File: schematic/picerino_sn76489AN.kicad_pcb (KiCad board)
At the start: 2 copper layers, 83.8 x 53.5 mm, 23 parts, among them CON1 PICERINO-EDGE, J1 Conn_01x02, J2 Conn_01x02, J3 Conn_01x02, U1 sn76489an, U2 74LS00, U3 LM386, Y1 3.579545Mhz

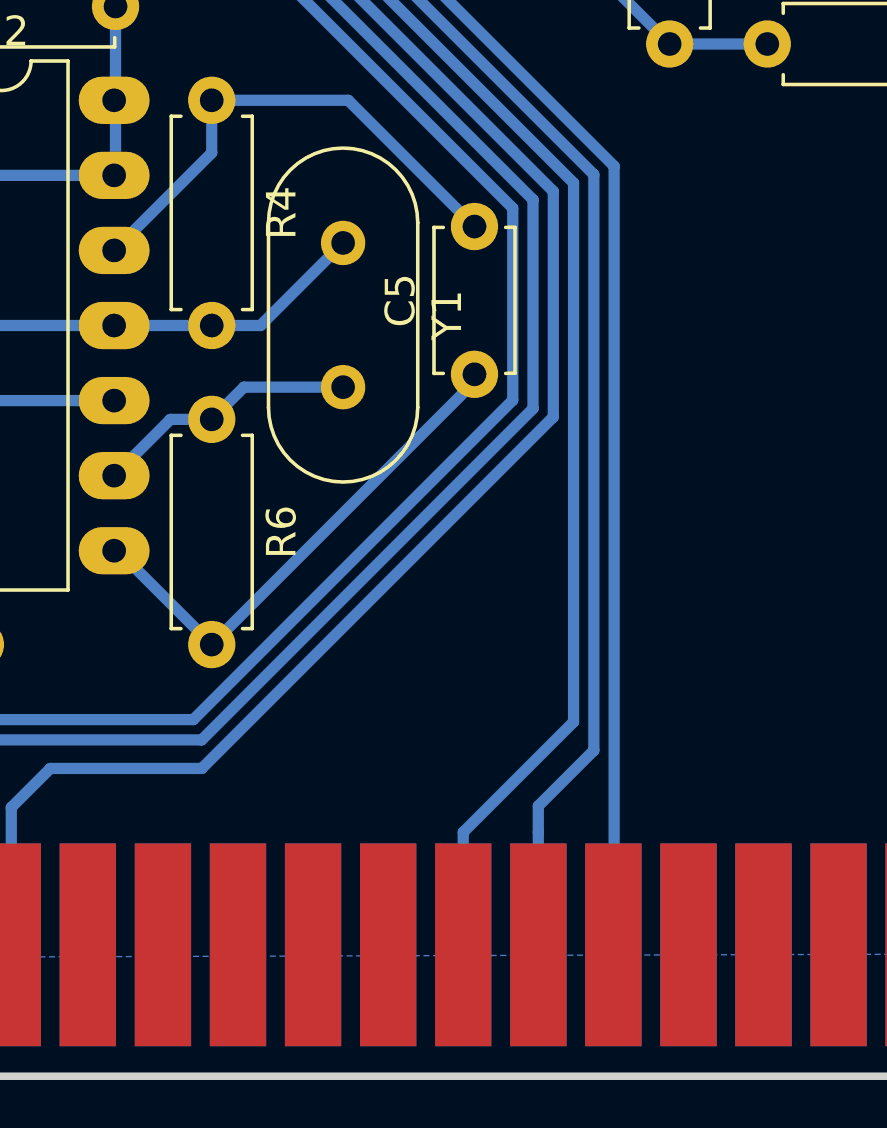
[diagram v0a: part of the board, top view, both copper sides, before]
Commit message: updated kicad schematic and pcb so ready is tied to RC7
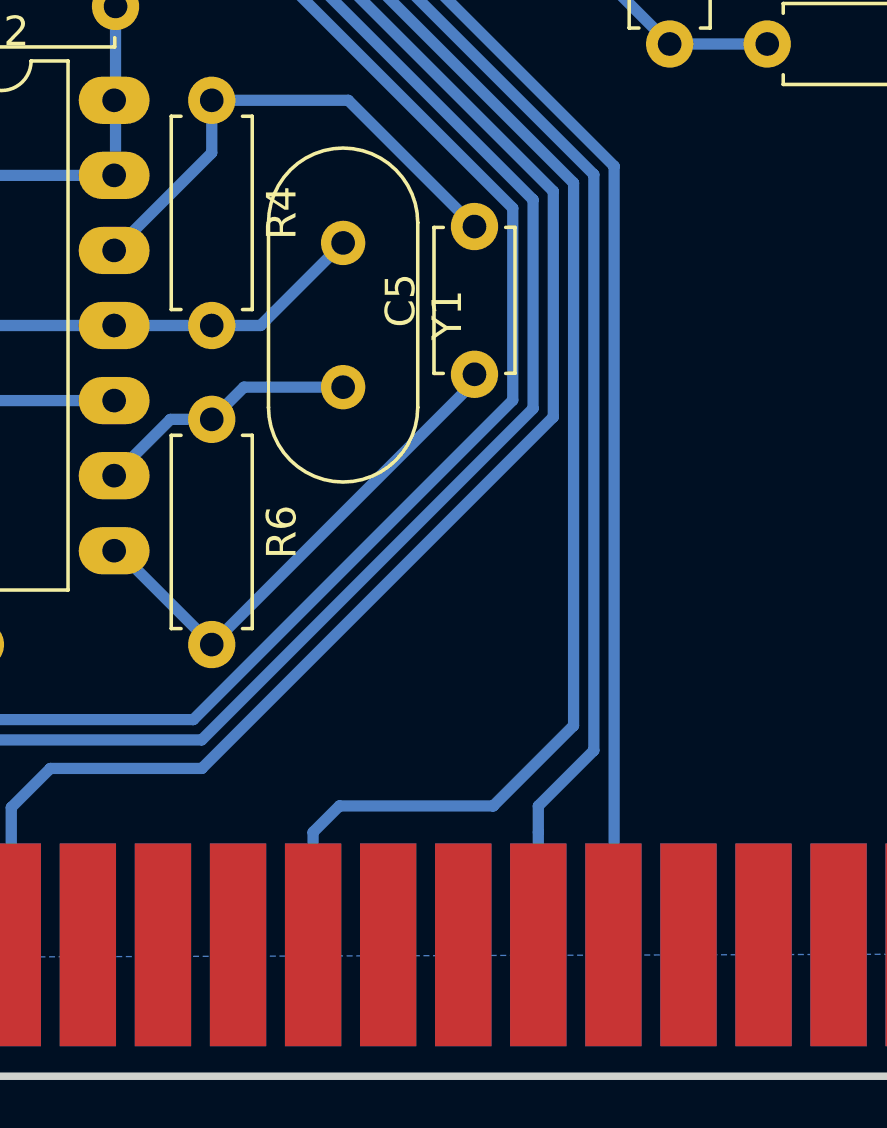
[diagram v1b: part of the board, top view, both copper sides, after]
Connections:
- R7 pad 1: Net-(CON1-PadA19) -> Net-(CON1-PadA17)
- U1 pad 4: Net-(CON1-PadA19) -> Net-(CON1-PadA17)
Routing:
- net Net-(CON1-PadA17): track 0.00 -> 85.8 mm
- net Net-(CON1-PadA19): track 80.7 -> 0.00 mm

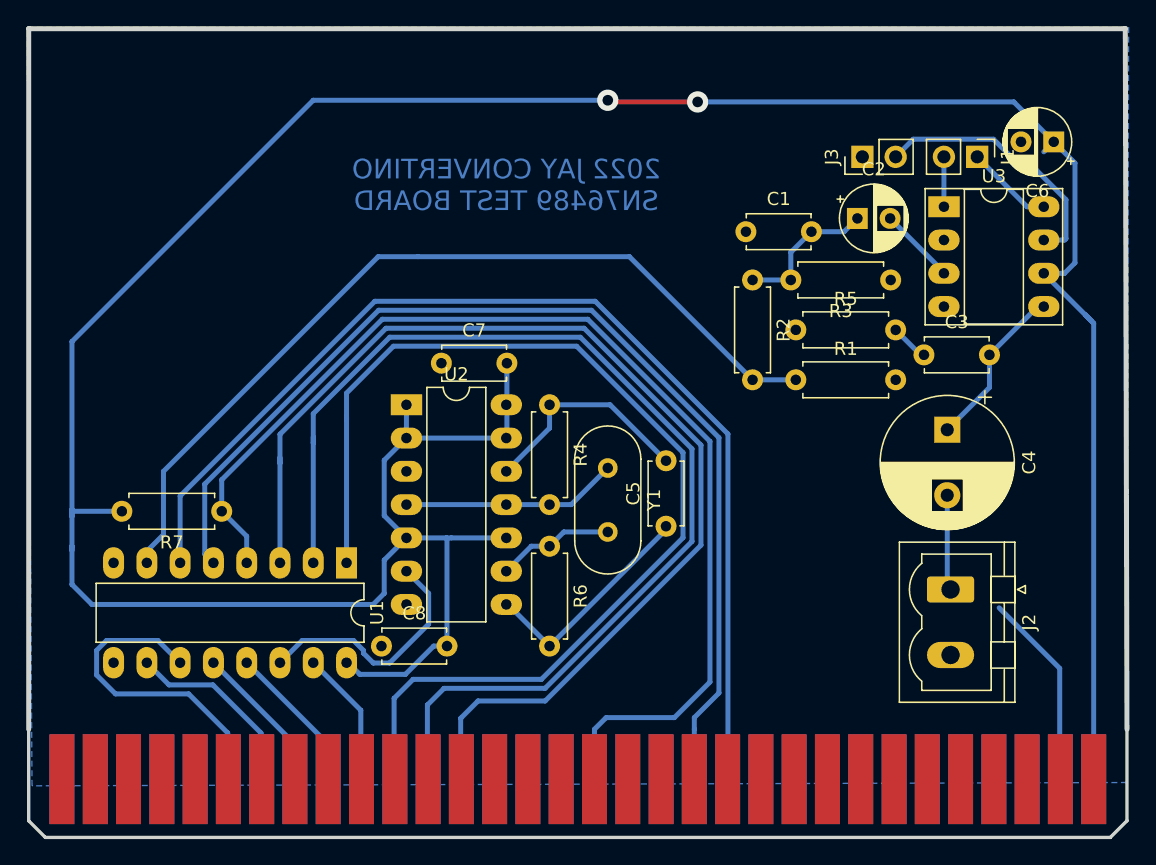
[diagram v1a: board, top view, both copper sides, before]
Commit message: reverse bit order on pcb to remove software reversal
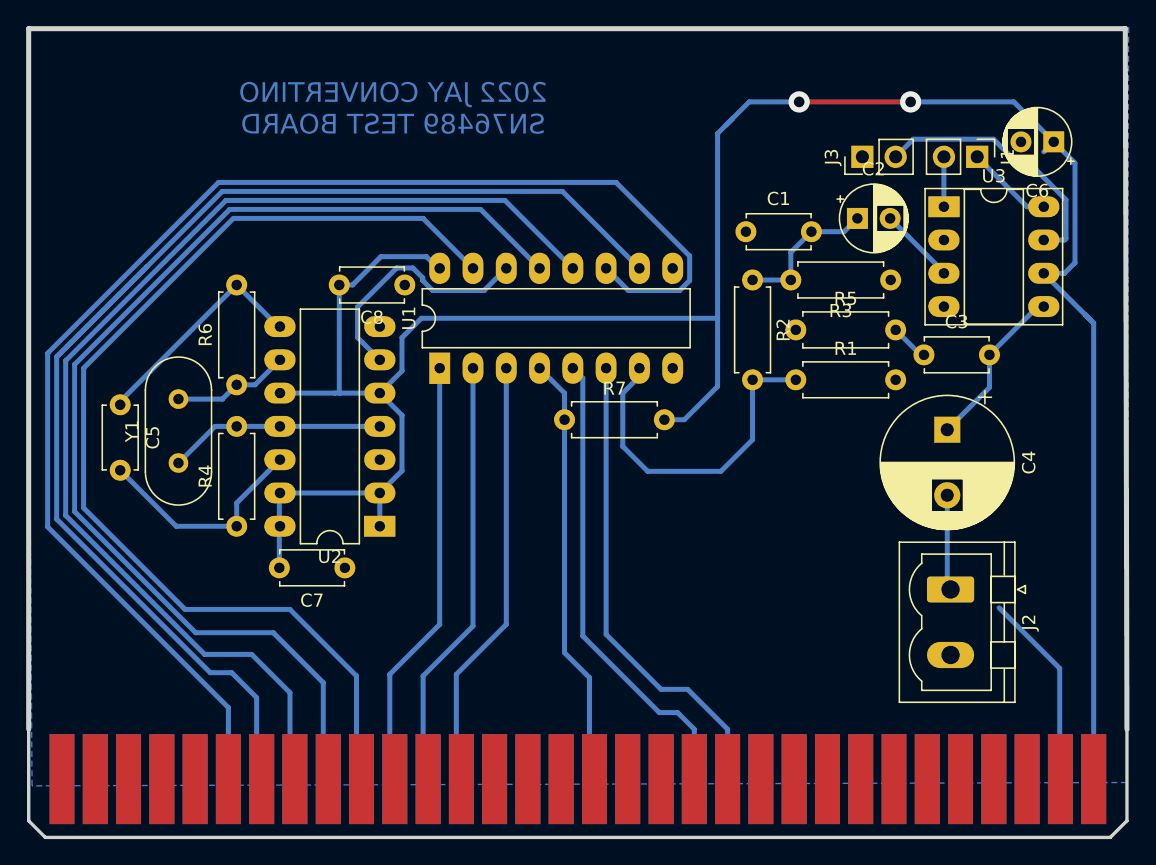
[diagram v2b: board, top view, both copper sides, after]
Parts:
- moved C5 42.7 mm to (113.9, 79.4), turned to 270 degrees
- moved Y1 32.8 mm to (118.4, 83.8), turned to 90 degrees
- moved C8 27.6 mm to (135.6, 70.2), turned to 180 degrees
- moved R7 27.1 mm to (147.8, 80.5), turned to 0 degrees
- moved R6 26.9 mm to (122.8, 77.9), turned to 90 degrees
- moved R4 25.6 mm to (122.8, 88.6), turned to 90 degrees
- moved C7 17.3 mm to (131.1, 91.8), turned to 180 degrees
- moved U1 16.5 mm to (138.3, 76.6), turned to 90 degrees
- moved U2 9.49 mm to (133.7, 88.6), turned to 180 degrees
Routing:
- net /D7: track 14.7 -> 101.5 mm
- net /D6: track 24.9 -> 104.2 mm
- net /D5: track 11.7 -> 87.2 mm
- net /D4: track 11.7 -> 85.4 mm
- net /D3: track 10.7 -> 80.9 mm
- net VCC: track 242.1 -> 187.9 mm
- net Net-(CON1-PadA17): track 85.8 -> 33.1 mm
- net /D0: track 85.8 -> 33.1 mm
- net /D1: track 85.1 -> 33.1 mm
- net /D2: track 83.8 -> 33.1 mm
- net Net-(CON1-PadA21): track 83.6 -> 39.1 mm
- net Net-(R1-Pad1): track 66.4 -> 26.1 mm
- net Net-(CON1-PadA20): track 81.9 -> 41.6 mm

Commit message: fixed pcb so bits are reversed as they should be
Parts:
- moved C5 42.6 mm to (156.2, 84.8), turned to 90 degrees
- moved Y1 33.6 mm to (151.8, 80.4), turned to 270 degrees
- moved R4 27.8 mm to (147.3, 75.6), turned to 270 degrees
- moved C7 26.4 mm to (149.0, 72.4)
- moved R6 25.9 mm to (147.3, 86.4), turned to 270 degrees
- moved C8 25.5 mm to (139.6, 95.4)
- moved R7 23.0 mm to (125.0, 83.4)
- moved U2 13.4 mm to (136.4, 75.6), turned to 0 degrees
- moved U1 12.8 mm to (131.8, 87.6), turned to 270 degrees
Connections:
- CON1 pad A10: /D3 -> /D4
- CON1 pad A11: /D2 -> /D5
- CON1 pad A12: /D1 -> /D6
- CON1 pad A13: /D0 -> /D7
- CON1 pad A6: /D6 -> /D1
- CON1 pad A7: /D7 -> /D0
- CON1 pad A8: /D5 -> /D2
- CON1 pad A9: /D4 -> /D3
- R7 pad 1: Net-(CON1-PadA17) -> Net-(CON1-PadA5)
- U1 pad 4: Net-(CON1-PadA17) -> Net-(CON1-PadA5)
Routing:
- net /D7: track 101.5 -> 31.3 mm
- net /D6: track 104.2 -> 41.7 mm
- net Net-(CON1-PadA21): track 39.1 -> 90.2 mm, vias 0 -> 2
- net Net-(CON1-PadA5): track 0.00 -> 45.3 mm
- net Net-(CON1-PadA20): track 41.6 -> 86.5 mm, vias 0 -> 2
- net Net-(R1-Pad1): track 26.1 -> 70.3 mm
- net /D5: track 87.2 -> 43.6 mm
- net /D4: track 85.4 -> 45.8 mm
- net Net-(CON1-PadA17): track 33.1 -> 0.00 mm
- net /D3: track 80.9 -> 50.4 mm
- net VCC: track 187.9 -> 159.7 mm
- net GNDD: track 15.8 -> 36.4 mm
- net /D2: track 33.1 -> 53.6 mm
- net /D1: track 33.1 -> 49.7 mm
- net /D0: track 33.1 -> 47.1 mm
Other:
- net class Default: trace_width 0.381 -> 0.3048
